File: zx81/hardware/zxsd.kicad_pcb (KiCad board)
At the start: 2 copper layers, 69.9 x 96.1 mm, 36 parts, among them J1 Micro_SD_Card, J2 ZX81_EXP, SW1 RESET, U1 74HCT32, U10 27C256, U11 KM62256CLP, U2 74HCT32, U3 74HCT00, U4 74HCT04, U5 74HCT163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

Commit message: optimized RAM OE generation (thanks to Sigi)
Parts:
- removed R5: 10k, Resistor_THT:R_Axial_DIN0207_L6.3mm_D2.5mm_P10.16mm_Horizontal
- added D2: BAT43, Diode_THT:D_DO-35_SOD27_P7.62mm_Horizontal, F.Cu at (137.2, 86.9)
- added D3: BAT43, Diode_THT:D_DO-35_SOD27_P7.62mm_Horizontal, F.Cu at (170.3, 99.8)
- added R6: 4k7, Resistor_THT:R_Axial_DIN0207_L6.3mm_D2.5mm_P10.16mm_Horizontal, F.Cu at (115.6, 90.2)
- moved C11 0.13 mm to (165.1, 86.9)
- moved C12 0.13 mm to (144.8, 86.9)
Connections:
- U11 pad 22: /nCS_RAM -> /nOE_RAM
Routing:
- net /nOE_RAM: track 0.00 -> 82.0 mm, vias 0 -> 5
- net /nWR: track 110.1 -> 96.3 mm
- net /nRD: track 72.5 -> 82.2 mm
- net /nRFSH: track 67.8 -> 71.6 mm, vias 1 -> 2
- net /nCS_RAM: track 49.5 -> 47.6 mm, vias 4 -> 2
- net GND: vias 87 -> 88

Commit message: some cosmetical fixes
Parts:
- moved R1 3.30 mm to (115.6, 90.7)
- moved R6 3.30 mm to (115.6, 86.9)
- moved D1 3.30 mm to (122.6, 97.0)
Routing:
- net Net-(R1-Pad2): track 82.2 -> 78.9 mm
- net /nOE_RAM: track 82.0 -> 79.0 mm, vias 5 -> 4
- net GND: vias 88 -> 87
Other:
- board text added: "ZX81 SD card Interface V1.3 (c) 2022 S. Ittner"
- board text removed: "ZX81 SD card Interface V1.2 (c) 2022 S. Ittner"

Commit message: re-fixed external ROM/EEPROM timing issue
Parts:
- removed JP4: DIS_INT_ROM, Jumper:SolderJumper-2_P1.3mm_Bridged_RoundedPad1.0x1.5mm
- added D4: BAT43, Diode_THT:D_DO-35_SOD27_P2.54mm_Vertical_AnodeUp, F.Cu at (177.8, 126.4)
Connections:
- U2 pad 2: Net-(U2-Pad2) -> /nMREQ
- U2 pad 5: Net-(U2-Pad2) -> Net-(U4-Pad6)
- U4 pad 6: Net-(U2-Pad2) -> Net-(U4-Pad6)
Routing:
- net /nMREQ: track 82.9 -> 136.1 mm, vias 3 -> 7
- net Net-(U2-Pad2): track 39.4 -> 0.00 mm, vias 2 -> 0
- net Net-(U4-Pad6): track 0.00 -> 27.7 mm
- net +5V: track 387.5 -> 380.0 mm, vias 19 -> 18
- net /nROMCS_INT: track 6.81 -> 9.94 mm, vias 1 -> 0
- net /nRFSH: track 71.6 -> 72.7 mm
- net GND: vias 87 -> 89
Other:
- board text removed: "DIS_INT_ROM"

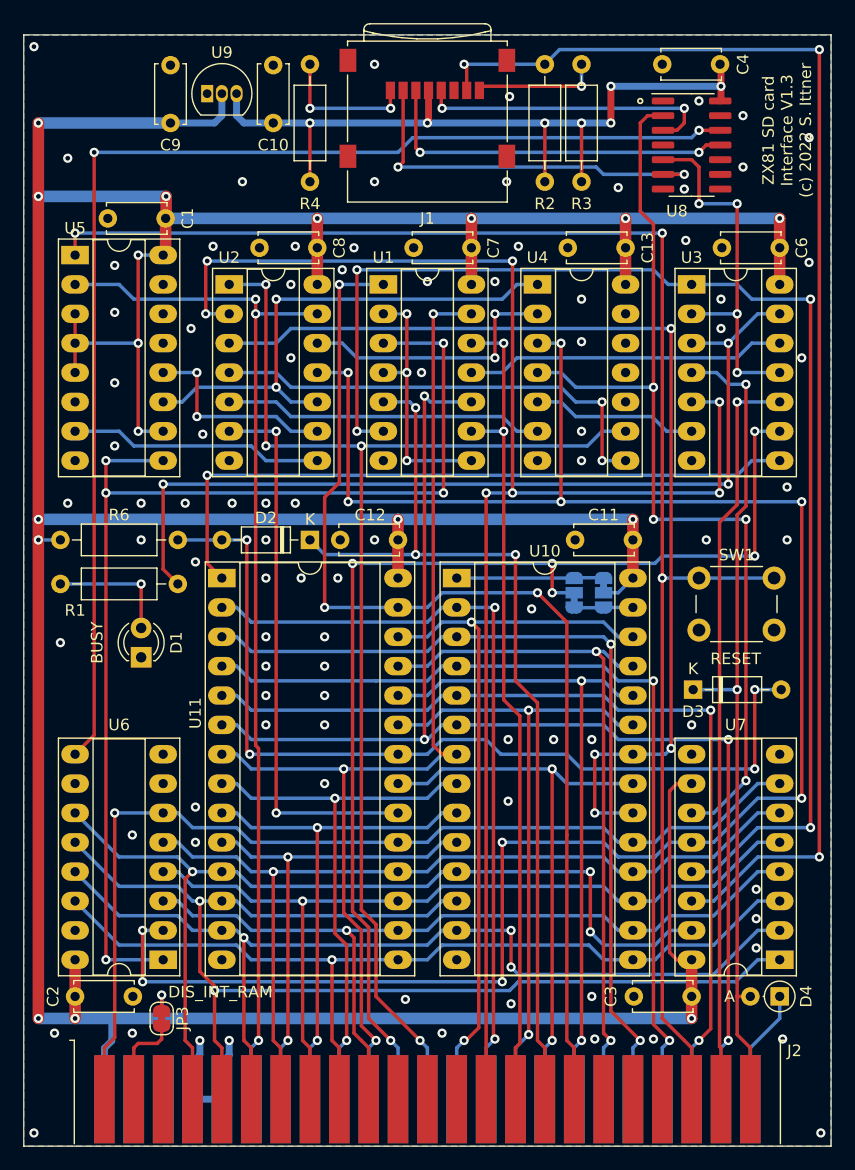
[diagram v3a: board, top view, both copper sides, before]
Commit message: full decoder logic finished
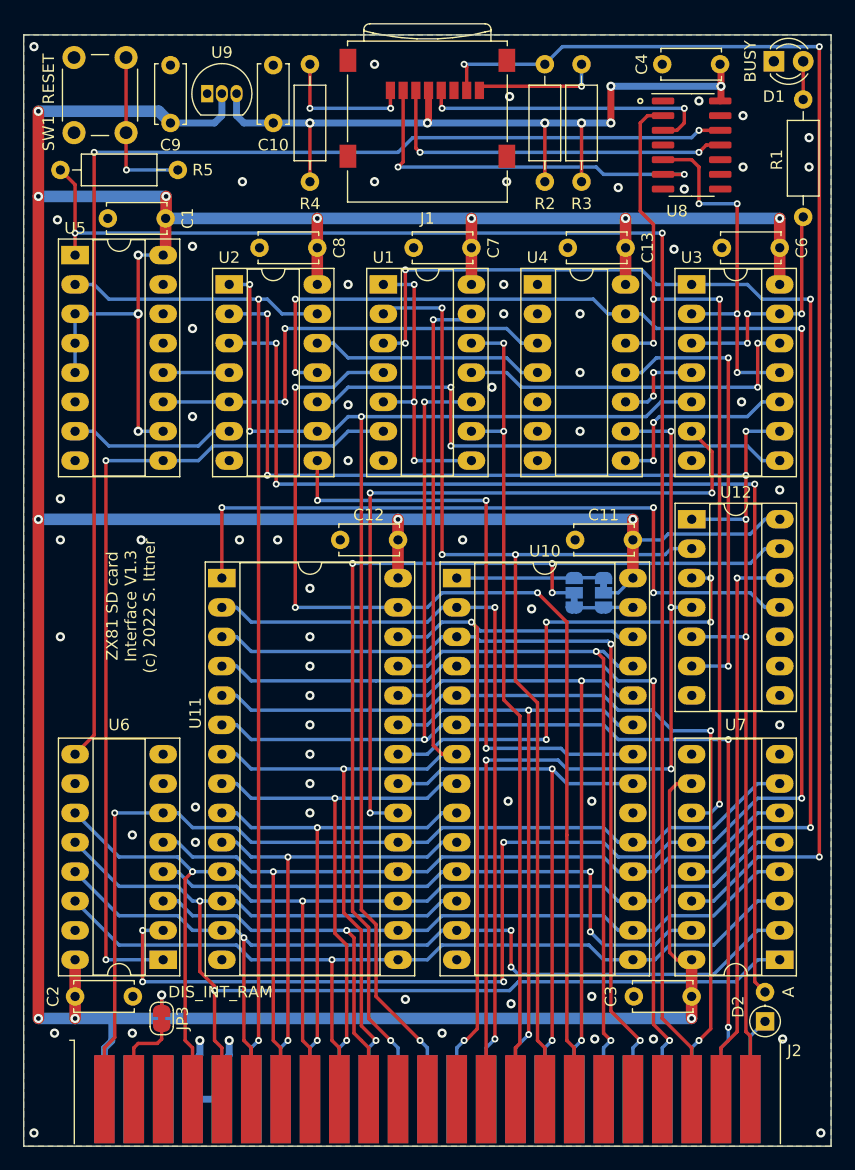
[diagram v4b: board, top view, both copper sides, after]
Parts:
- removed D3: BAT43, Diode_THT:D_DO-35_SOD27_P7.62mm_Horizontal
- removed D4: BAT43, Diode_THT:D_DO-35_SOD27_P2.54mm_Vertical_AnodeUp
- removed R6: 4k7, Resistor_THT:R_Axial_DIN0207_L6.3mm_D2.5mm_P10.16mm_Horizontal
- added R5: 100R, Resistor_THT:R_Axial_DIN0207_L6.3mm_D2.5mm_P10.16mm_Horizontal, F.Cu at (125.7, 54.9)
- added U12: 74HCT08, Package_DIP:DIP-14_W7.62mm_Socket_LongPads, F.Cu at (170.2, 85.1)
- D2: footprint Diode_THT:D_DO-35_SOD27_P7.62mm_Horizontal -> Diode_THT:D_DO-35_SOD27_P2.54mm_Vertical_AnodeUp
- moved R1 76.7 mm to (179.8, 48.8), turned to -90 degrees
- moved D1 75.2 mm to (177.3, 45.5), turned to 0 degrees
- moved SW1 67.0 mm to (121.2, 45.1), turned to -90 degrees
- moved D2 57.3 mm to (176.5, 128.5), turned to 90 degrees
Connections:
- D2 pad 1: /nRD -> /nROMCS_INT
- D2 pad 2: /nOE_RAM -> Net-(D2-Pad2)
- SW1 pad 1: /nRESET -> Net-(R5-Pad1)
- U1 pad 1: /nWR -> Net-(U1-Pad5)
- U1 pad 2: Net-(U1-Pad2) -> /nRD
- U1 pad 3: /nSDWR -> /nSDRD
- U1 pad 4: Net-(U1-Pad2) -> /nWR
- U1 pad 5: /nRD -> Net-(U1-Pad5)
- U1 pad 6: /nSDRD -> /nSDWR
- U1 pad 8: Net-(U1-Pad2) -> Net-(U1-Pad5)
- U10 pad 20: /nCS_ROM -> GND
- U2 pad 10: Net-(U2-Pad10) -> Net-(U3-Pad8)
- U2 pad 12: Net-(U2-Pad12) -> Net-(U4-Pad4)
- U2 pad 2: /nMREQ -> /nRFSH
- U2 pad 3: /nCS_ROM -> Net-(D2-Pad2)
- U2 pad 4: Net-(U4-Pad8) -> Net-(U5-Pad12)
- U2 pad 5: Net-(U4-Pad6) -> Net-(U2-Pad5)
- U2 pad 6: /nCS_RAM -> Net-(U5-Pad7)
- U2 pad 8: Net-(U2-Pad8) -> /nCS_ROM
- U2 pad 9: Net-(U2-Pad9) -> /A14
- U3 pad 10: /nM1 -> Net-(U3-Pad10)
- U3 pad 4: /nRFSH -> Net-(U3-Pad4)
- U3 pad 5: /nMREQ -> /A14
- U3 pad 6: Net-(U3-Pad6) -> /nCS_RAM
- U3 pad 8: Net-(U11-Pad1) -> Net-(U3-Pad8)
- U3 pad 9: /A15 -> /nRFSH
- U4 pad 1: Net-(U2-Pad10) -> GND
- U4 pad 10: unconnected-(U4-Pad10) -> Net-(U3-Pad4)
- U4 pad 11: GND -> Net-(U12-Pad6)
- U4 pad 12: unconnected-(U4-Pad12) -> /SD_CLK
- U4 pad 13: GND -> /nSD_CLK
- U4 pad 2: Net-(U2-Pad12) -> unconnected-(U4-Pad2)
- U4 pad 3: /nSD_CLK -> Net-(U2-Pad5)
- U4 pad 4: /SD_CLK -> Net-(U4-Pad4)
- U4 pad 5: Net-(U3-Pad6) -> GND
- U4 pad 6: Net-(U4-Pad6) -> unconnected-(U4-Pad6)
- U4 pad 8: Net-(U4-Pad8) -> Net-(U3-Pad10)
- U4 pad 9: /A14 -> /nMREQ
- U5 pad 11: Net-(U2-Pad10) -> Net-(U2-Pad5)
- U5 pad 12: Net-(U2-Pad9) -> Net-(U5-Pad12)
- U5 pad 7: Net-(U2-Pad8) -> Net-(U5-Pad7)
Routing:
- net Net-(D2-Pad2): track 0.00 -> 102.0 mm, vias 0 -> 3
- net Net-(R1-Pad2): track 78.9 -> 20.5 mm
- net /nRFSH: track 72.7 -> 128.9 mm, vias 2 -> 6
- net /nMREQ: track 136.1 -> 80.6 mm, vias 7 -> 4
- net Net-(U3-Pad8): track 0.00 -> 46.1 mm, vias 0 -> 2
- net Net-(U2-Pad10): track 45.1 -> 0.00 mm, vias 2 -> 0
- net Net-(U4-Pad8): track 40.4 -> 0.00 mm, vias 2 -> 0
- net Net-(U2-Pad5): track 0.00 -> 39.3 mm, vias 0 -> 2
- net Net-(U12-Pad6): track 0.00 -> 39.3 mm, vias 0 -> 2
- net /nCS_ROM: track 90.3 -> 52.4 mm, vias 4 -> 3
- net /nOE_RAM: track 79.0 -> 43.2 mm
- net Net-(U4-Pad6): track 27.7 -> 0.00 mm
- net /nSDWR: track 100.5 -> 73.2 mm, vias 5 -> 2
- net Net-(U1-Pad5): track 0.00 -> 25.5 mm, vias 0 -> 3
- net Net-(U2-Pad12): track 23.4 -> 0.00 mm, vias 2 -> 0
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
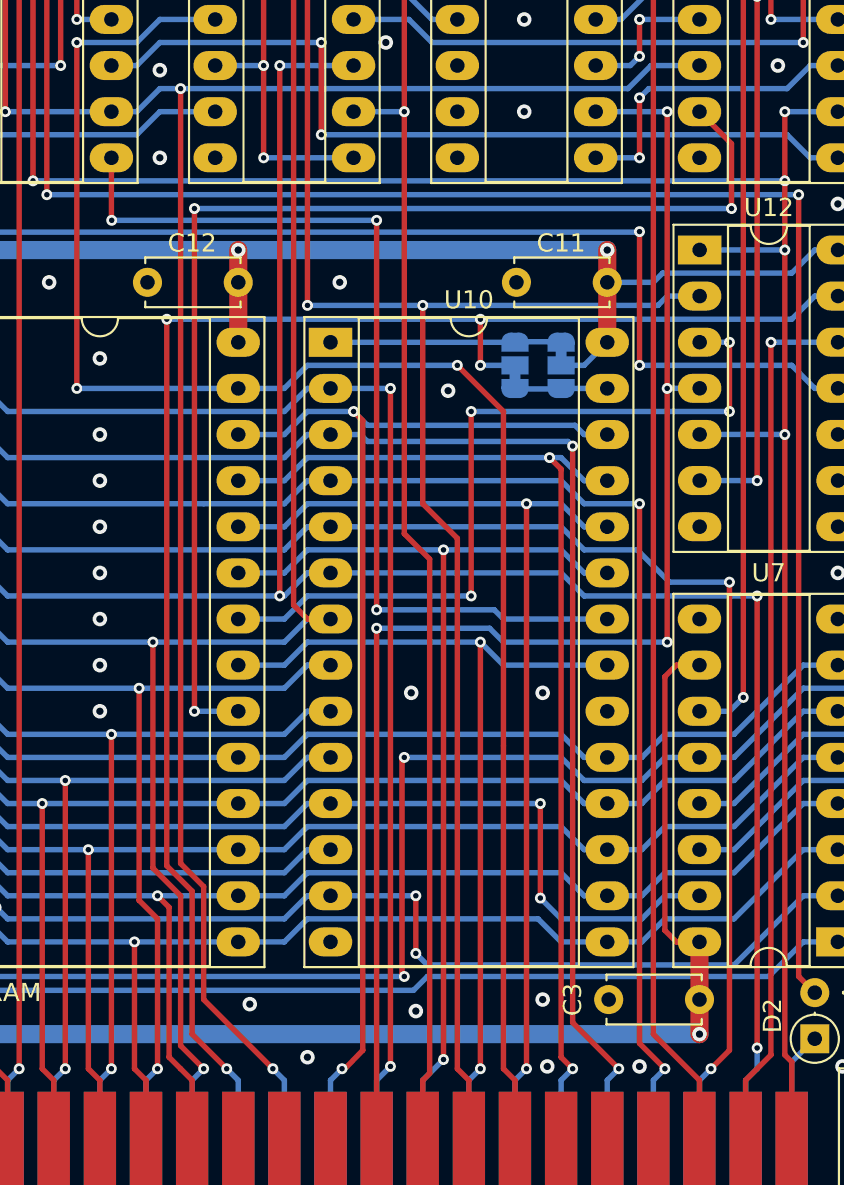
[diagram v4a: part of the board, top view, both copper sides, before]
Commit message: re-used ROM's /CE for address decoder, /RD is connected to /OE now
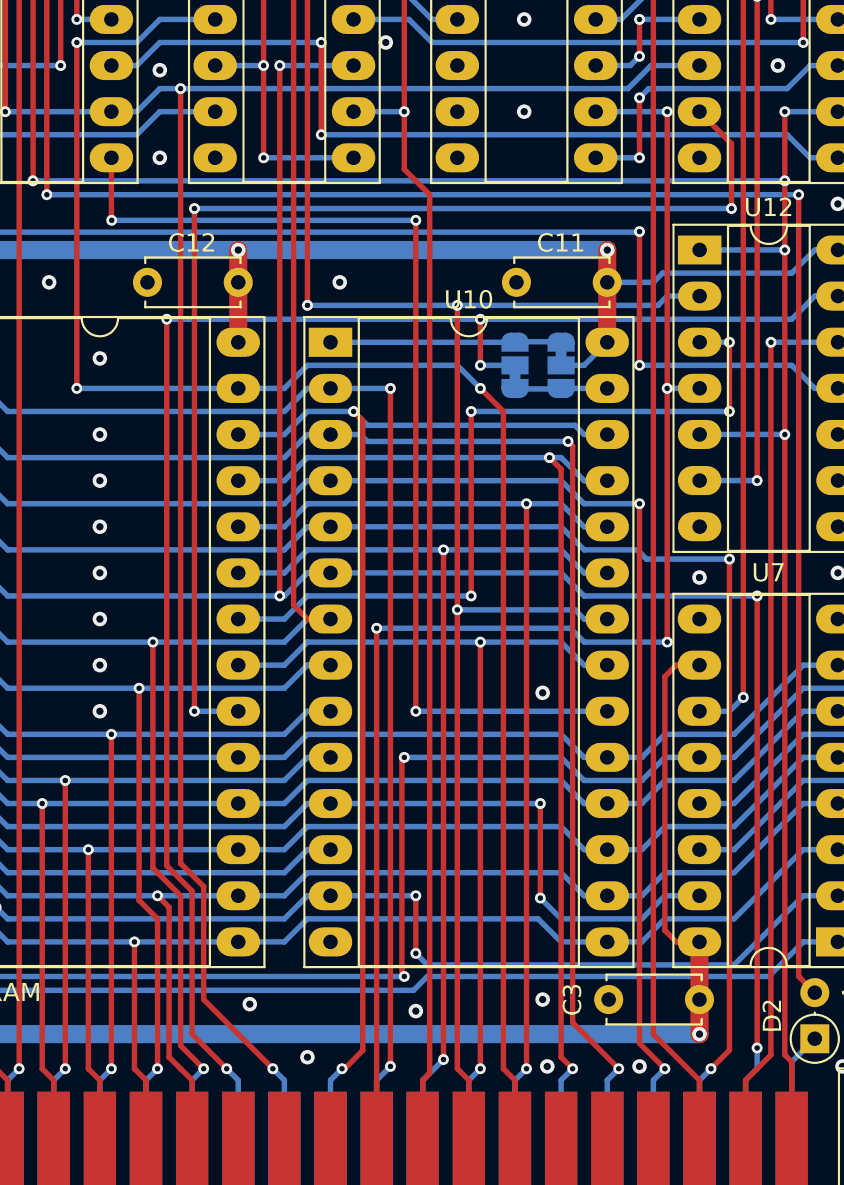
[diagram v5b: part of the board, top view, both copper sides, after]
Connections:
- U10 pad 20: GND -> /nCS_ROM
- U10 pad 22: /nCS_ROM -> /nRD
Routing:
- net /nRD: track 96.6 -> 104.3 mm, vias 3 -> 4
- net /nCS_ROM: track 52.4 -> 57.8 mm
- net /A5: track 77.2 -> 77.9 mm
- net GND: vias 64 -> 63
